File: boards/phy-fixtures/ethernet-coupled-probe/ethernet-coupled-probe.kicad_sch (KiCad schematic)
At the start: 58 parts, among them J1 RJ45, J10 SMA, J11 SMA, J12 SMA, J13 SMA, J14 SMA, J15 SMA, J16 SMA, J17 SMA, J18 SMA, J2 RJ45, J3 SMA, J4 SMA, J5 SMA, J6 SMA, J7 SMA, J8 SMA, J9 SMA, U1 DBTC16-282LX+, U10 DBTC16-282LX+, U11 DBTC16-282LX+, U12 DBTC16-282LX+, U13 DBTC16-282LX+, U14 DBTC16-282LX+, U15 DBTC16-282LX+, U16 DBTC16-282LX+, U2 DBTC16-282LX+, U3 DBTC16-282LX+, U4 DBTC16-282LX+, U5 DBTC16-282LX+, U6 DBTC16-282LX+, U7 DBTC16-282LX+, U8 DBTC16-282LX+, U9 DBTC16-282LX+

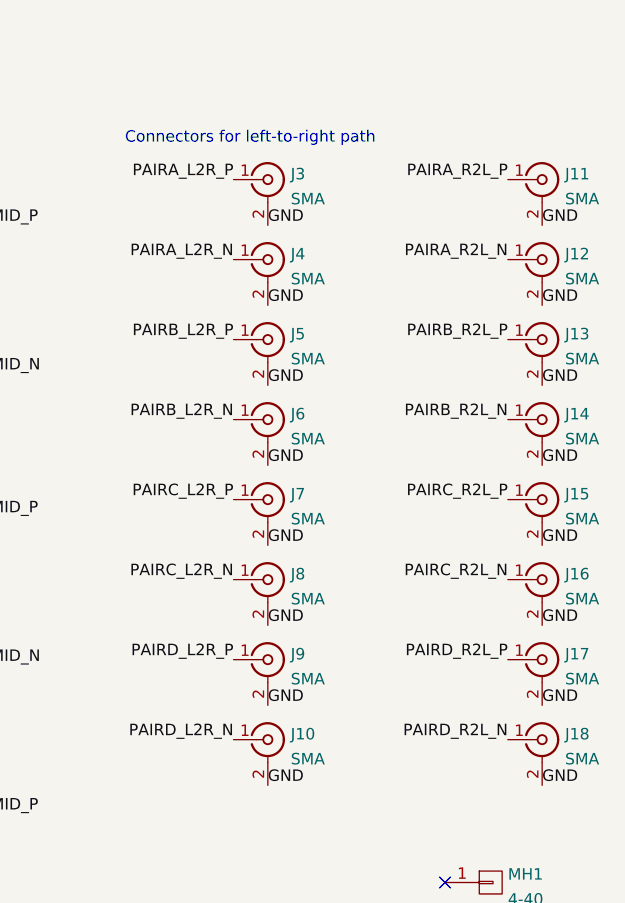
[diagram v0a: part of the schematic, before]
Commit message: Updated ethernet-coupled-probe for v0.2 with correct coupler footprint
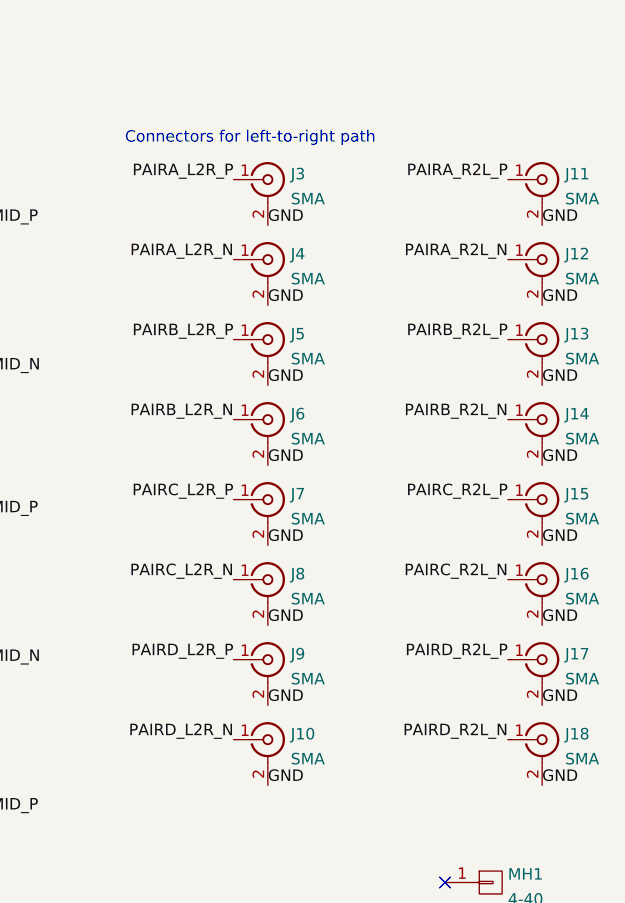
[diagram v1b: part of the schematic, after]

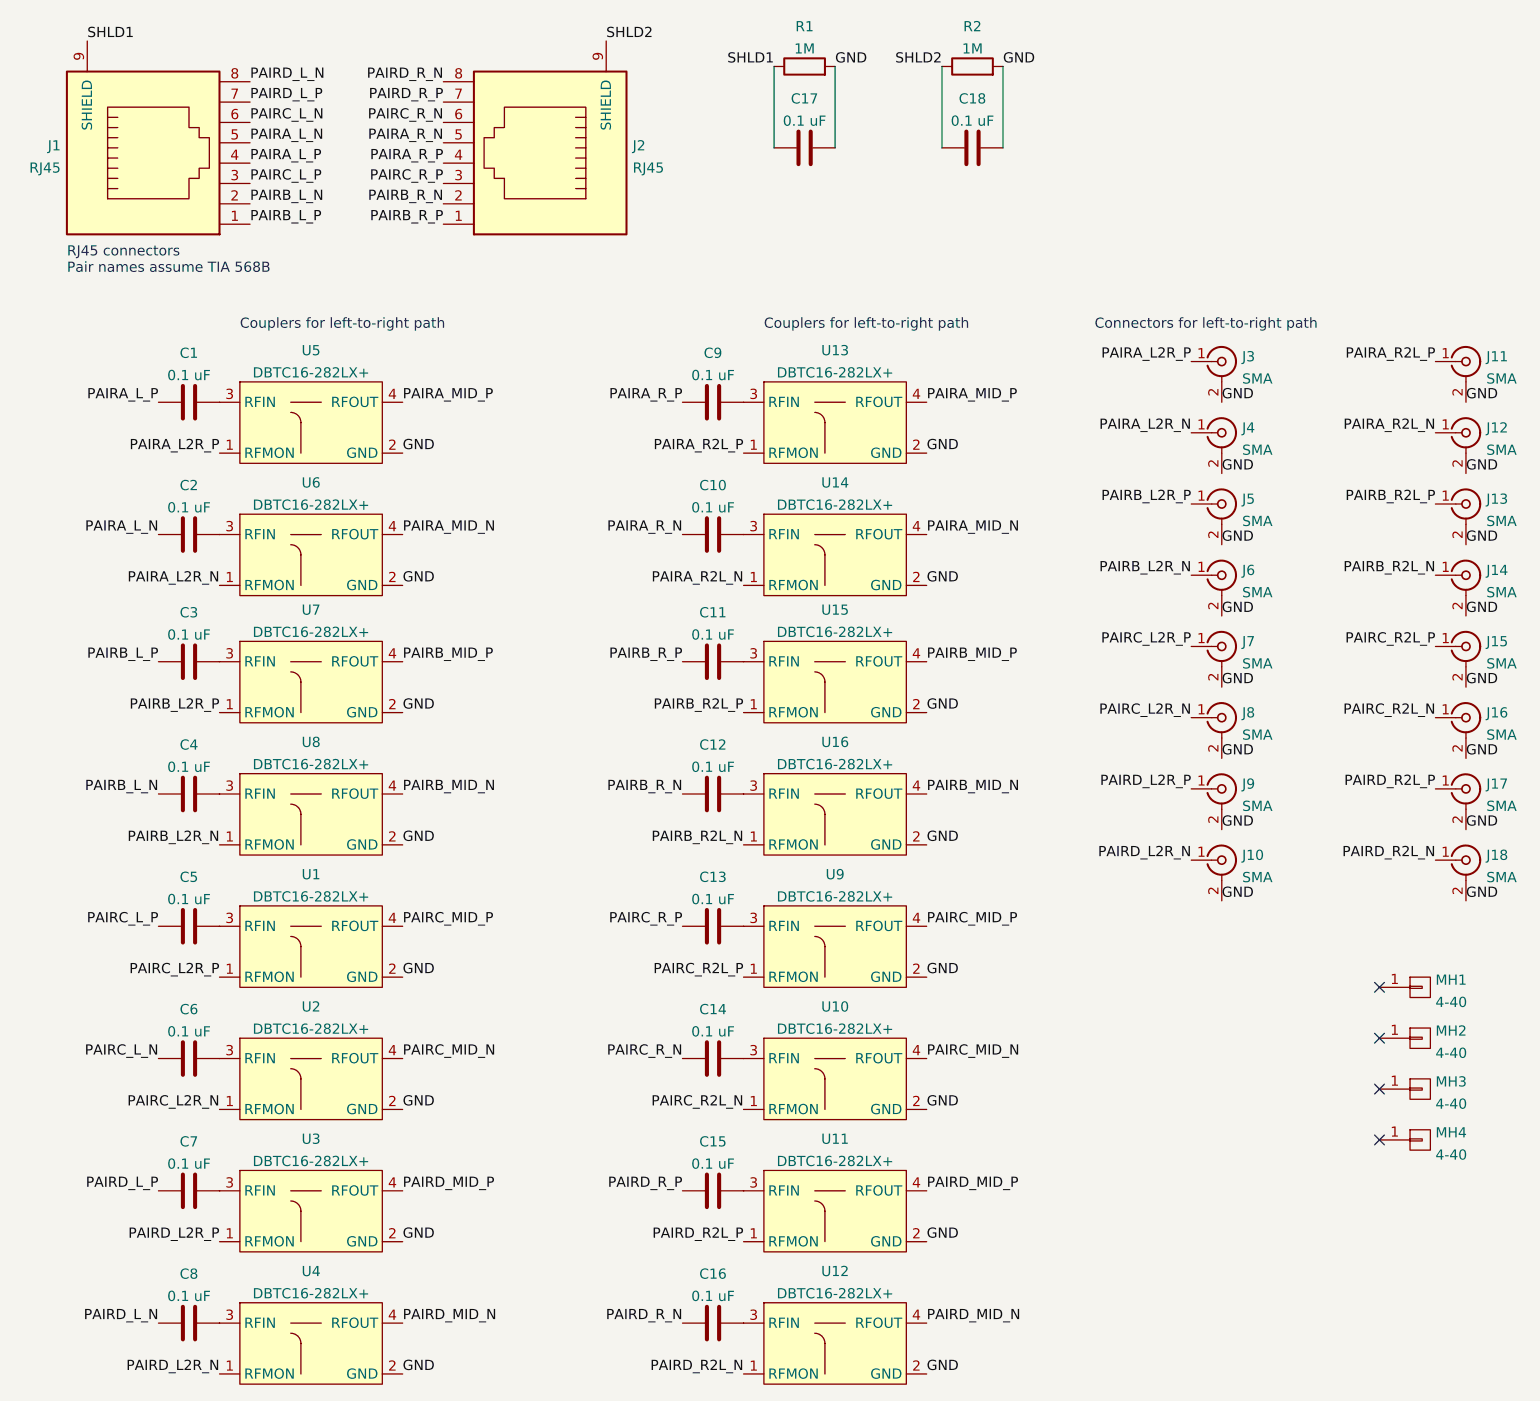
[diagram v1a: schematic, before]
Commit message: ethernet-coupled-probe: updated silkscreen and schematic with new net names for correct pinout. No changes to copper geometry.
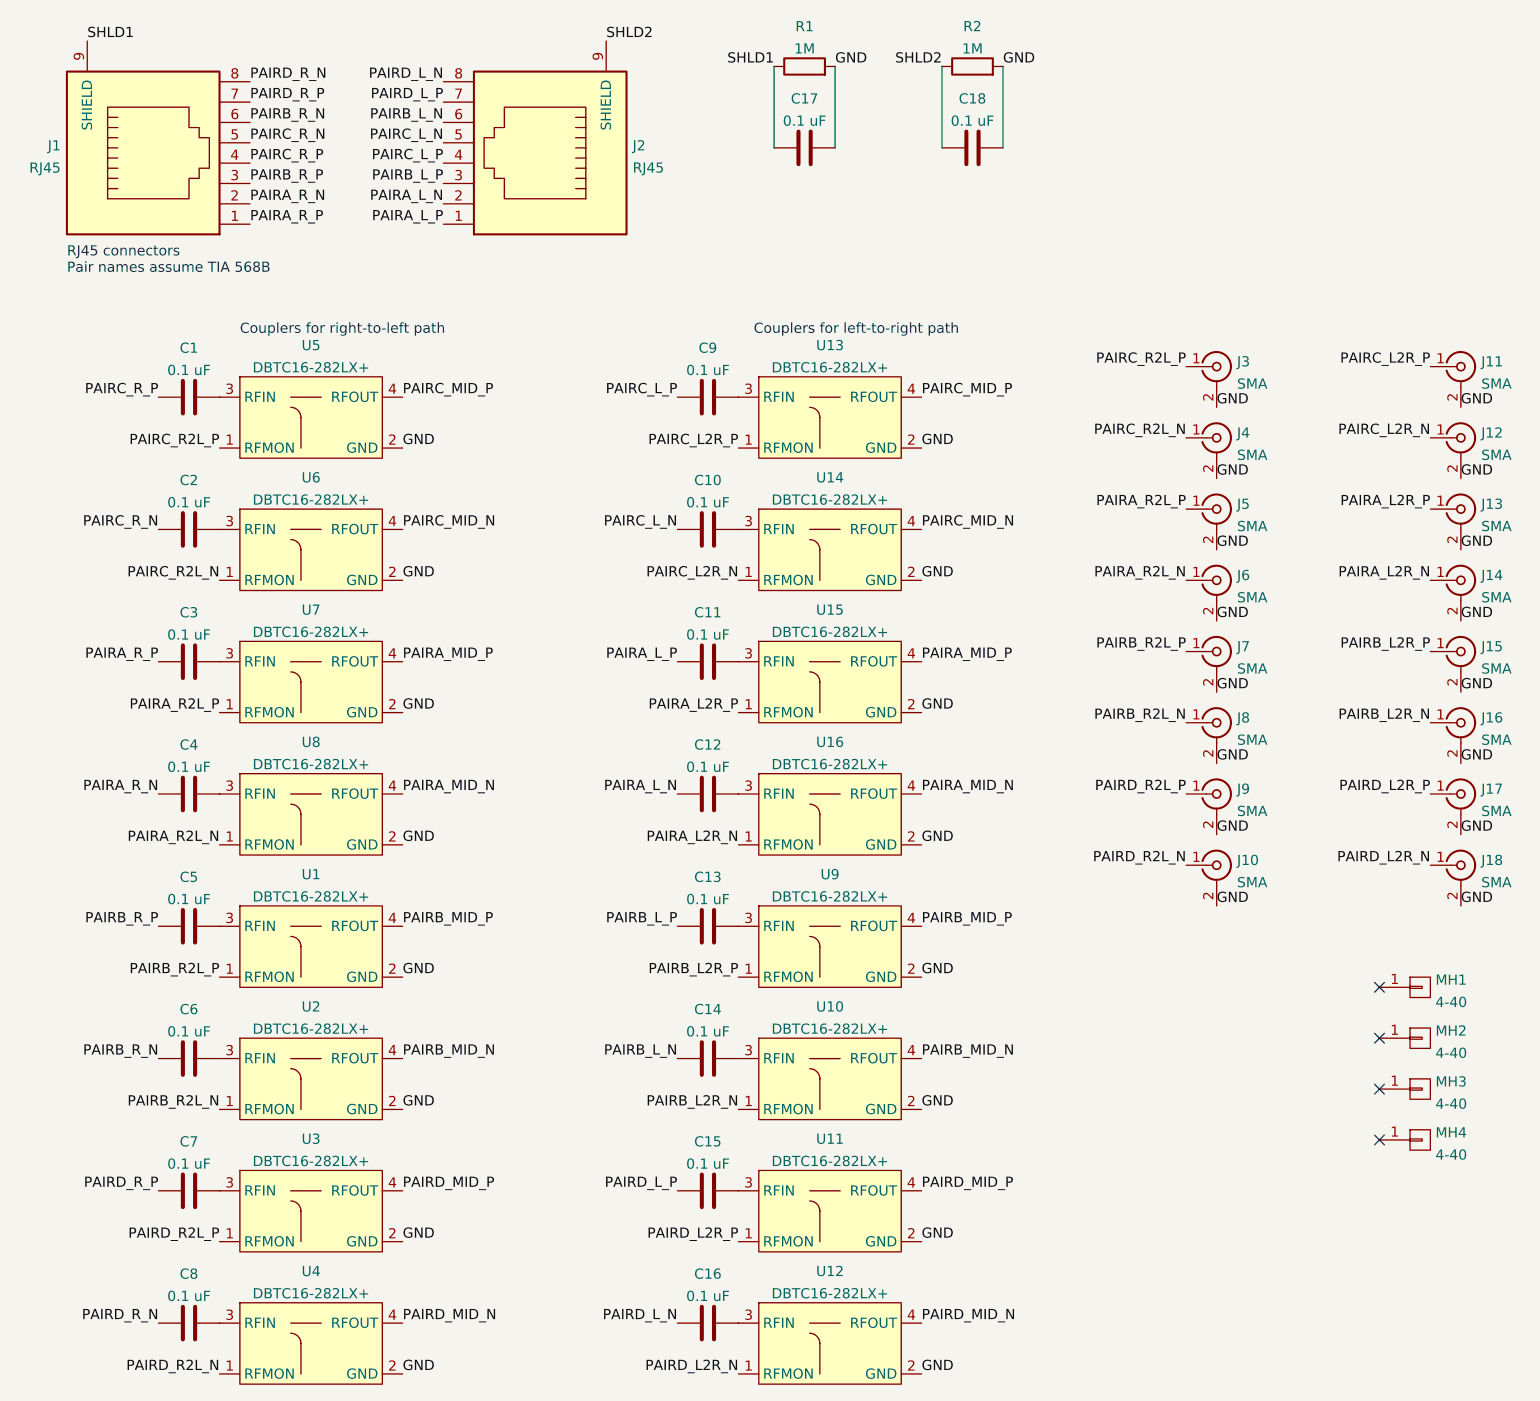
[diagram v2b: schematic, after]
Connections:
- net PAIRA_L2R_N: now also J14.1 (In), U16.1 (RFMON); no longer J4.1 (In), U6.1 (RFMON)
- net PAIRA_L2R_P: now also J13.1 (In), U15.1 (RFMON); no longer J3.1 (In), U5.1 (RFMON)
- net PAIRA_L_N: now also C12.1, J2.2; no longer C2.1, J1.5
- net PAIRA_L_P: now also C11.1, J2.1; no longer C1.1, J1.4
- net PAIRA_MID_N: now also U16.4 (RFOUT), U8.4 (RFOUT); no longer U14.4 (RFOUT), U6.4 (RFOUT)
- net PAIRA_MID_P: now also U15.4 (RFOUT), U7.4 (RFOUT); no longer U13.4 (RFOUT), U5.4 (RFOUT)
- net PAIRA_R2L_N: now also J6.1 (In), U8.1 (RFMON); no longer J12.1 (In), U14.1 (RFMON)
- net PAIRA_R2L_P: now also J5.1 (In), U7.1 (RFMON); no longer J11.1 (In), U13.1 (RFMON)
- net PAIRA_R_N: now also C4.1, J1.2; no longer C10.1, J2.5
- net PAIRA_R_P: now also C3.1, J1.1; no longer C9.1, J2.4
- net PAIRB_L2R_N: now also J16.1 (In), U10.1 (RFMON); no longer J6.1 (In), U8.1 (RFMON)
- net PAIRB_L2R_P: now also J15.1 (In), U9.1 (RFMON); no longer J5.1 (In), U7.1 (RFMON)
- net PAIRB_L_N: now also C14.1, J2.6; no longer C4.1, J1.2
- net PAIRB_L_P: now also C13.1, J2.3; no longer C3.1, J1.1
- net PAIRB_MID_N: now also U10.4 (RFOUT), U2.4 (RFOUT); no longer U16.4 (RFOUT), U8.4 (RFOUT)
- net PAIRB_MID_P: now also U1.4 (RFOUT), U9.4 (RFOUT); no longer U15.4 (RFOUT), U7.4 (RFOUT)
- net PAIRB_R2L_N: now also J8.1 (In), U2.1 (RFMON); no longer J14.1 (In), U16.1 (RFMON)
- net PAIRB_R2L_P: now also J7.1 (In), U1.1 (RFMON); no longer J13.1 (In), U15.1 (RFMON)
- net PAIRB_R_N: now also C6.1, J1.6; no longer C12.1, J2.2
- net PAIRB_R_P: now also C5.1, J1.3; no longer C11.1, J2.1
- net PAIRC_L2R_N: now also J12.1 (In), U14.1 (RFMON); no longer J8.1 (In), U2.1 (RFMON)
- net PAIRC_L2R_P: now also J11.1 (In), U13.1 (RFMON); no longer J7.1 (In), U1.1 (RFMON)
- net PAIRC_L_N: now also C10.1, J2.5; no longer C6.1, J1.6
- net PAIRC_L_P: now also C9.1, J2.4; no longer C5.1, J1.3
- net PAIRC_MID_N: now also U14.4 (RFOUT), U6.4 (RFOUT); no longer U10.4 (RFOUT), U2.4 (RFOUT)
- net PAIRC_MID_P: now also U13.4 (RFOUT), U5.4 (RFOUT); no longer U1.4 (RFOUT), U9.4 (RFOUT)
- net PAIRC_R2L_N: now also J4.1 (In), U6.1 (RFMON); no longer J16.1 (In), U10.1 (RFMON)
- net PAIRC_R2L_P: now also J3.1 (In), U5.1 (RFMON); no longer J15.1 (In), U9.1 (RFMON)
- net PAIRC_R_N: now also C2.1, J1.5; no longer C14.1, J2.6
- net PAIRC_R_P: now also C1.1, J1.4; no longer C13.1, J2.3
- net PAIRD_L2R_N: now also J18.1 (In), U12.1 (RFMON); no longer J10.1 (In), U4.1 (RFMON)
- net PAIRD_L2R_P: now also J17.1 (In), U11.1 (RFMON); no longer J9.1 (In), U3.1 (RFMON)
- net PAIRD_L_N: now also C16.1, J2.8; no longer C8.1, J1.8
- net PAIRD_L_P: now also C15.1, J2.7; no longer C7.1, J1.7
- net PAIRD_R2L_N: now also J10.1 (In), U4.1 (RFMON); no longer J18.1 (In), U12.1 (RFMON)
- net PAIRD_R2L_P: now also J9.1 (In), U3.1 (RFMON); no longer J17.1 (In), U11.1 (RFMON)
- net PAIRD_R_N: now also C8.1, J1.8; no longer C16.1, J2.8
- net PAIRD_R_P: now also C7.1, J1.7; no longer C15.1, J2.7
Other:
- note added: "Couplers for right-to-left path"
- note removed: "Connectors for left-to-right path"
- moved on the sheet: C1, C10, C11, C12, C13, C14, C15, C16, C2, C9, J10, J11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
